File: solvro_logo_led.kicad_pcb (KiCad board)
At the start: 2 copper layers, 33 parts

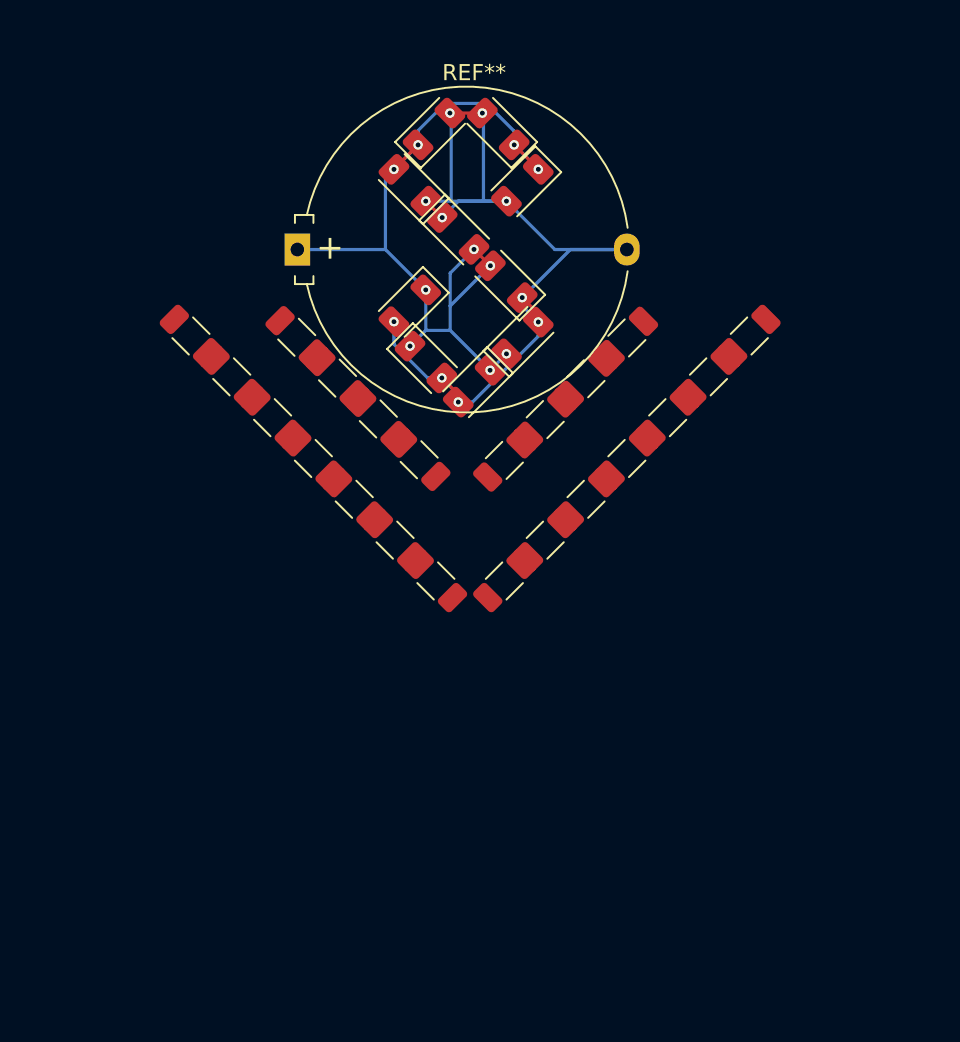
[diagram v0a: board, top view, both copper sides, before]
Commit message: Zmiany rezystorów na ledy
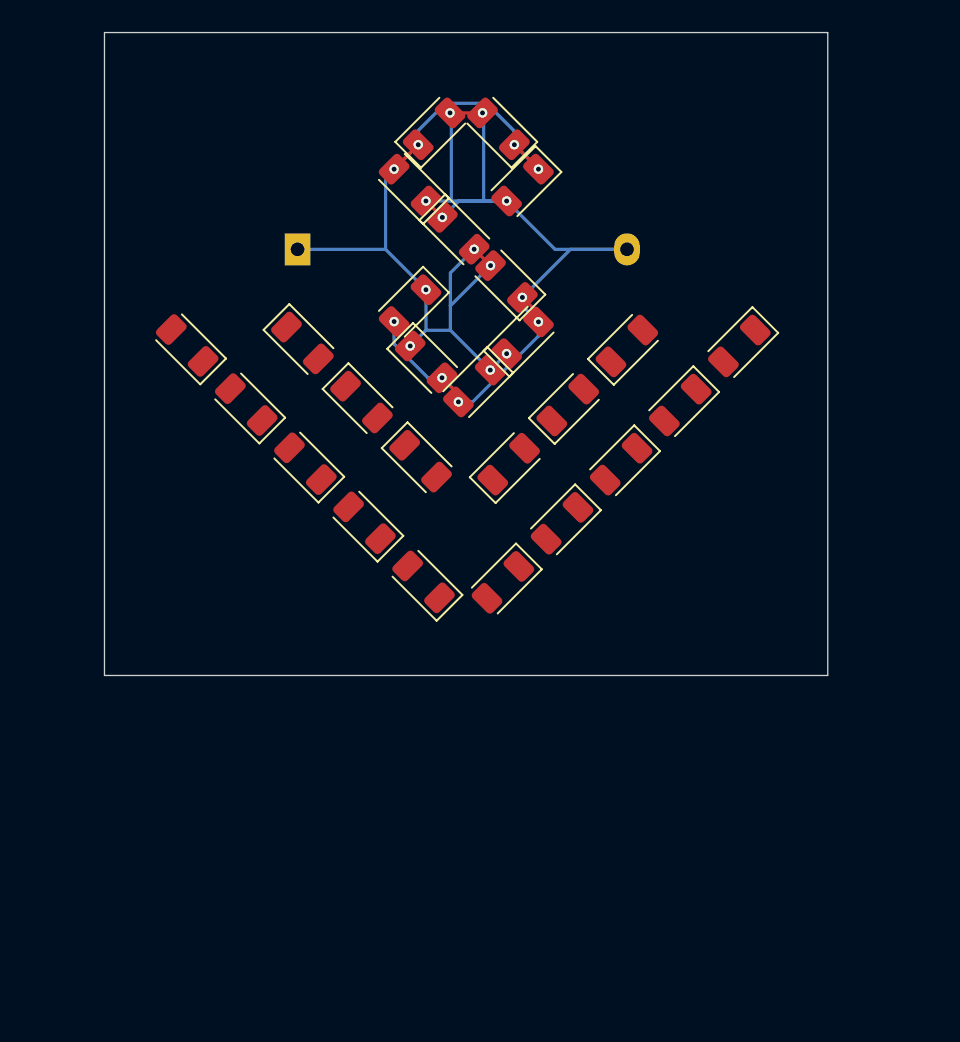
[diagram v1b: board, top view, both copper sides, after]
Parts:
- removed the REF** at (172.5, 82.0)
- removed the REF** at (167.1, 93.1)
- removed the REF** at (166.5, 83.5)
- removed the REF** at (170.5, 88.5)
- removed the REF** at (166.5, 76.0)
- removed the REF** at (173.5, 85.5)
- removed the REF** at (169.5, 79.0)
- removed the REF** at (168.1, 100.6)
- removed the REF** at (167.5, 87.0)
- removed the REF** at (172.0, 72.5)
- removed the REF** at (180.0, 85.5)
- removed the REF** at (168.0, 72.5)
- removed the REF** at (173.5, 76.0)
- removed the REF** at (187.6, 85.4)
- removed REF**1 (x2), REF**2 (x2), REF**3 (x2), REF**4 (x2), REF**5 (x2), REF**6 (x2), REF**7 (x2), REF**8 (x2), REF**9 (x2): R_1206_3216Metric, Resistor_SMD:R_1206_3216Metric
- added REF**: LED_1206_3216Metric, LED_SMD:LED_1206_3216Metric, F.Cu at (170.5, 88.5)
- added REF**: LED_1206_3216Metric, LED_SMD:LED_1206_3216Metric, F.Cu at (166.5, 83.5)
- added REF**: LED_1206_3216Metric, LED_SMD:LED_1206_3216Metric, F.Cu at (173.5, 85.5)
- added REF**: LED_1206_3216Metric, LED_SMD:LED_1206_3216Metric, F.Cu at (172.5, 82.0)
- added REF**: LED_1206_3216Metric, LED_SMD:LED_1206_3216Metric, F.Cu at (172.0, 72.5)
- added REF**: LED_1206_3216Metric, LED_SMD:LED_1206_3216Metric, F.Cu at (173.5, 76.0)
- added REF**: LED_1206_3216Metric, LED_SMD:LED_1206_3216Metric, F.Cu at (168.0, 72.5)
- added REF**: LED_1206_3216Metric, LED_SMD:LED_1206_3216Metric, F.Cu at (187.0, 86.0)
- added REF**: LED_1206_3216Metric, LED_SMD:LED_1206_3216Metric, F.Cu at (169.5, 79.0)
- added REF**: LED_1206_3216Metric, LED_SMD:LED_1206_3216Metric, F.Cu at (167.5, 87.0)
- added REF**: LED_1206_3216Metric, LED_SMD:LED_1206_3216Metric, F.Cu at (167.4, 100.7)
- added REF**: LED_1206_3216Metric, LED_SMD:LED_1206_3216Metric, F.Cu at (166.5, 76.0)
- added REF**10: LED_1206_3216Metric, LED_SMD:LED_1206_3216Metric, F.Cu at (183.3, 89.7)
- added REF**10: LED_1206_3216Metric, LED_SMD:LED_1206_3216Metric, F.Cu at (163.7, 97.0)
- added REF**11: LED_1206_3216Metric, LED_SMD:LED_1206_3216Metric, F.Cu at (179.6, 93.4)
- added REF**11: LED_1206_3216Metric, LED_SMD:LED_1206_3216Metric, F.Cu at (160.0, 93.3)
- added REF**12: LED_1206_3216Metric, LED_SMD:LED_1206_3216Metric, F.Cu at (156.3, 89.6)
- added REF**12: LED_1206_3216Metric, LED_SMD:LED_1206_3216Metric, F.Cu at (176.0, 97.0)
- added REF**13: LED_1206_3216Metric, LED_SMD:LED_1206_3216Metric, F.Cu at (180.0, 86.0)
- added REF**13: LED_1206_3216Metric, LED_SMD:LED_1206_3216Metric, F.Cu at (167.2, 93.2)
- added REF**13: LED_1206_3216Metric, LED_SMD:LED_1206_3216Metric, F.Cu at (152.6, 86.0)
- added REF**13: LED_1206_3216Metric, LED_SMD:LED_1206_3216Metric, F.Cu at (172.3, 100.7)
- added REF**14: LED_1206_3216Metric, LED_SMD:LED_1206_3216Metric, F.Cu at (163.5, 89.5)
- added REF**14: LED_1206_3216Metric, LED_SMD:LED_1206_3216Metric, F.Cu at (176.3, 89.7)
- added REF**15: LED_1206_3216Metric, LED_SMD:LED_1206_3216Metric, F.Cu at (159.8, 85.8)
- added REF**15: LED_1206_3216Metric, LED_SMD:LED_1206_3216Metric, F.Cu at (172.6, 93.4)
- REF**: moved to B.Cu
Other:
- board outline added: 45 x 40 mm

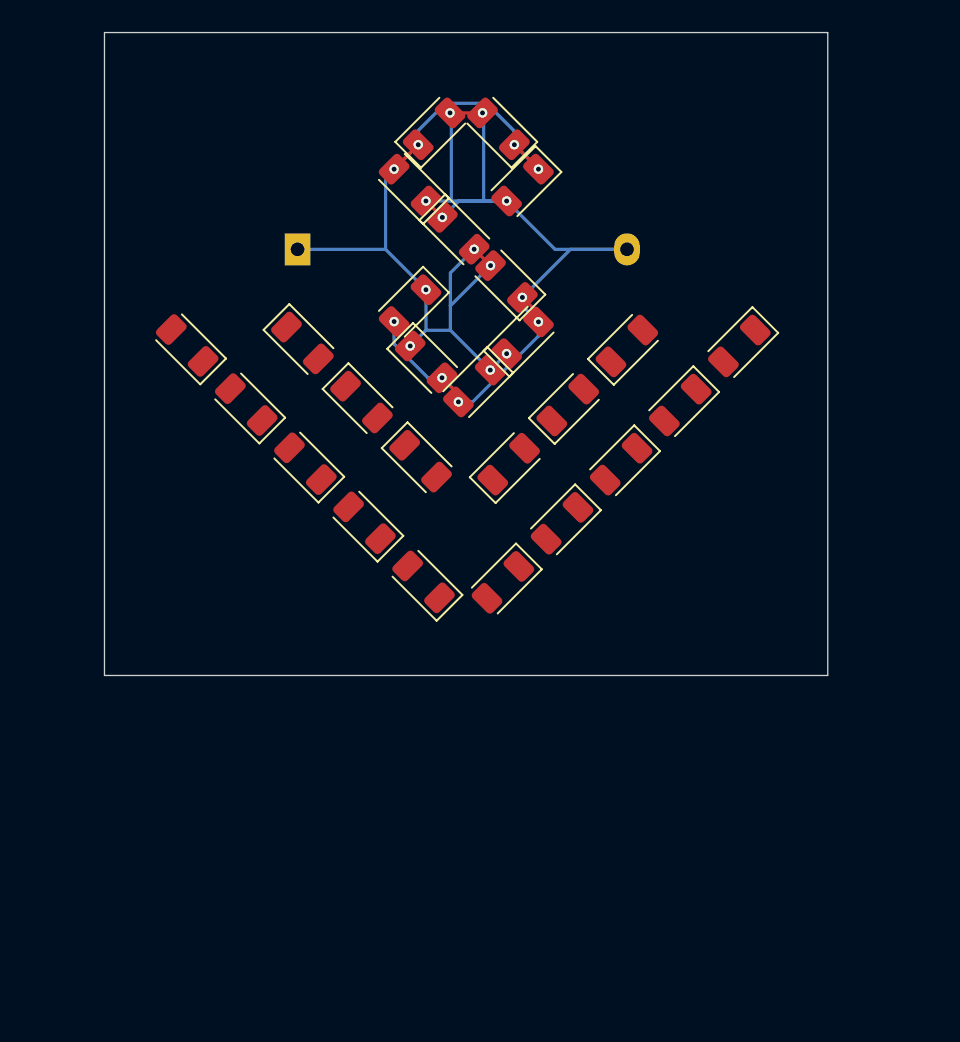
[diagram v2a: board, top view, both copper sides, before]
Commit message: Dodanie plików gerber, schematu, płytki produkcyjnej i stp
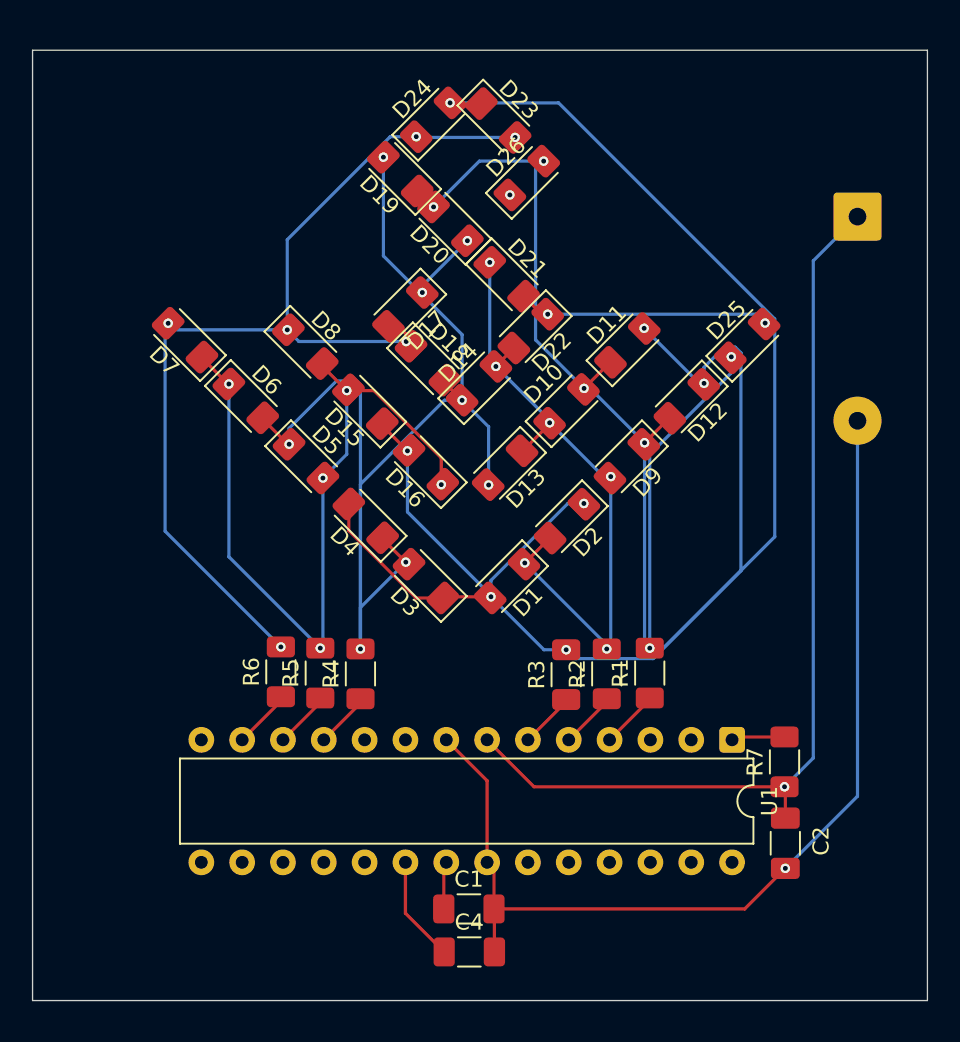
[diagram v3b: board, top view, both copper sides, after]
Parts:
- removed REF** (x12), REF**10 (x2), REF**11 (x2), REF**12 (x2), REF**13 (x4), REF**14 (x2), REF**15 (x2): LED_1206_3216Metric, LED_SMD:LED_1206_3216Metric
- removed REF**: Battery_Panasonic_CR2032-HFN_Horizontal_CircularHoles, Battery:Battery_Panasonic_CR2032-HFN_Horizontal_CircularHoles
- added BT1: 4.5V Battery, Battery:BatteryHolder_Keystone_2479_3xAAA, B.Cu at (194.3, 78.0)
- added C1: 100nF, Capacitor_SMD:C_1206_3216Metric_Pad1.33x1.80mm_HandSolder, F.Cu at (170.2, 121.0)
- added C2: 100nF, Capacitor_SMD:C_1206_3216Metric_Pad1.33x1.80mm_HandSolder, F.Cu at (189.9, 116.9)
- added C4: 10uF, Capacitor_SMD:C_1206_3216Metric_Pad1.33x1.80mm_HandSolder, F.Cu at (170.2, 123.7)
- added D1: LED, LED_SMD:LED_1206_3216Metric_Pad1.42x1.75mm_HandSolder, F.Cu at (172.5, 100.6)
- added D10: LED, LED_SMD:LED_1206_3216Metric_Pad1.42x1.75mm_HandSolder, F.Cu at (176.2, 89.8)
- added D11: LED, LED_SMD:LED_1206_3216Metric_Pad1.42x1.75mm_HandSolder, F.Cu at (180.0, 86.0)
- added D12: LED, LED_SMD:LED_1206_3216Metric_Pad1.42x1.75mm_HandSolder, F.Cu at (183.7, 89.4)
- added D13: LED, LED_SMD:LED_1206_3216Metric_Pad1.42x1.75mm_HandSolder, F.Cu at (172.4, 93.6)
- added D14: LED, LED_SMD:LED_1206_3216Metric_Pad1.42x1.75mm_HandSolder, F.Cu at (170.8, 88.3)
- added D15: LED, LED_SMD:LED_1206_3216Metric_Pad1.42x1.75mm_HandSolder, F.Cu at (163.7, 89.8)
- added D16: LED, LED_SMD:LED_1206_3216Metric_Pad1.42x1.75mm_HandSolder, F.Cu at (167.5, 93.5)
- added D17: LED, LED_SMD:LED_1206_3216Metric_Pad1.42x1.75mm_HandSolder, F.Cu at (166.2, 83.7)
- added D18: LED, LED_SMD:LED_1206_3216Metric_Pad1.42x1.75mm_HandSolder, F.Cu at (167.6, 87.1)
- added D19: LED, LED_SMD:LED_1206_3216Metric_Pad1.42x1.75mm_HandSolder, F.Cu at (165.9, 75.3)
- added D2: LED, LED_SMD:LED_1206_3216Metric_Pad1.42x1.75mm_HandSolder, F.Cu at (176.3, 96.9)
- added D20: LED, LED_SMD:LED_1206_3216Metric_Pad1.42x1.75mm_HandSolder, F.Cu at (169.0, 78.4)
- added D21: LED, LED_SMD:LED_1206_3216Metric_Pad1.42x1.75mm_HandSolder, F.Cu at (172.5, 81.8)
- added D22: LED, LED_SMD:LED_1206_3216Metric_Pad1.42x1.75mm_HandSolder, F.Cu at (174.0, 85.1)
- added D23: LED, LED_SMD:LED_1206_3216Metric_Pad1.42x1.75mm_HandSolder, F.Cu at (172.0, 72.0)
- added D24: LED, LED_SMD:LED_1206_3216Metric_Pad1.42x1.75mm_HandSolder, F.Cu at (167.9, 71.9)
- added D25: LED, LED_SMD:LED_1206_3216Metric_Pad1.42x1.75mm_HandSolder, F.Cu at (187.5, 85.7)
- added D26: LED, LED_SMD:LED_1206_3216Metric_Pad1.42x1.75mm_HandSolder, F.Cu at (173.8, 75.6)
- added D3: LED, LED_SMD:LED_1206_3216Metric_Pad1.42x1.75mm_HandSolder, F.Cu at (167.5, 100.6)
- added D4: LED, LED_SMD:LED_1206_3216Metric_Pad1.42x1.75mm_HandSolder, F.Cu at (163.8, 96.9)
- added D5: LED, LED_SMD:LED_1206_3216Metric_Pad1.42x1.75mm_HandSolder, F.Cu at (160.0, 93.2)
- added D6: LED, LED_SMD:LED_1206_3216Metric_Pad1.42x1.75mm_HandSolder, F.Cu at (156.3, 89.4)
- added D7: LED, LED_SMD:LED_1206_3216Metric_Pad1.42x1.75mm_HandSolder, F.Cu at (152.5, 85.6)
- added D8: LED, LED_SMD:LED_1206_3216Metric_Pad1.42x1.75mm_HandSolder, F.Cu at (160.0, 86.0)
- added D9: LED, LED_SMD:LED_1206_3216Metric_Pad1.42x1.75mm_HandSolder, F.Cu at (180.0, 93.2)
- added R1: 47R, Resistor_SMD:R_1206_3216Metric_Pad1.30x1.75mm_HandSolder, F.Cu at (181.4, 106.3)
- added R2: 47R, Resistor_SMD:R_1206_3216Metric_Pad1.30x1.75mm_HandSolder, F.Cu at (178.8, 106.4)
- added R3: 47R, Resistor_SMD:R_1206_3216Metric_Pad1.30x1.75mm_HandSolder, F.Cu at (176.2, 106.5)
- added R4: 47R, Resistor_SMD:R_1206_3216Metric_Pad1.30x1.75mm_HandSolder, F.Cu at (163.4, 106.4)
- added R5: 47R, Resistor_SMD:R_1206_3216Metric_Pad1.30x1.75mm_HandSolder, F.Cu at (160.9, 106.3)
- added R6: 47R, Resistor_SMD:R_1206_3216Metric_Pad1.30x1.75mm_HandSolder, F.Cu at (158.5, 106.3)
- added R7: 10K, Resistor_SMD:R_1206_3216Metric_Pad1.30x1.75mm_HandSolder, F.Cu at (189.8, 111.9)
- added U1: ATmega328-P, Package_DIP:DIP-28_W7.62mm, F.Cu at (186.5, 110.5)
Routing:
- net Net-(D1-A): track 0.00 -> 127.8 mm, vias 0 -> 7
- net Net-(D13-A): track 0.00 -> 83.5 mm, vias 0 -> 8
- net Net-(D10-A): track 0.00 -> 68.0 mm, vias 0 -> 6
- net Net-(D15-A): track 0.00 -> 66.0 mm, vias 0 -> 8
- net Net-(BT1-+): track 0.00 -> 65.6 mm, vias 0 -> 1
- net Net-(BT1--): track 0.00 -> 63.3 mm, vias 0 -> 1
- net Net-(D17-A): track 0.00 -> 63.1 mm, vias 0 -> 6
- net LED-: track 60.9 -> 0.00 mm, vias 10 -> 0
- net LED+: track 52.9 -> 0.00 mm, vias 10 -> 0
- net Net-(D1-K): track 0.00 -> 41.3 mm, vias 0 -> 6
- net F: track 0.00 -> 3.68 mm
- net A: track 0.00 -> 3.64 mm
- net E: track 0.00 -> 3.57 mm
- net B: track 0.00 -> 3.53 mm
- net D: track 0.00 -> 3.50 mm
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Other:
- board size 45 x 40 mm -> 55.7 x 59.1 mm

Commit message: export to gerber
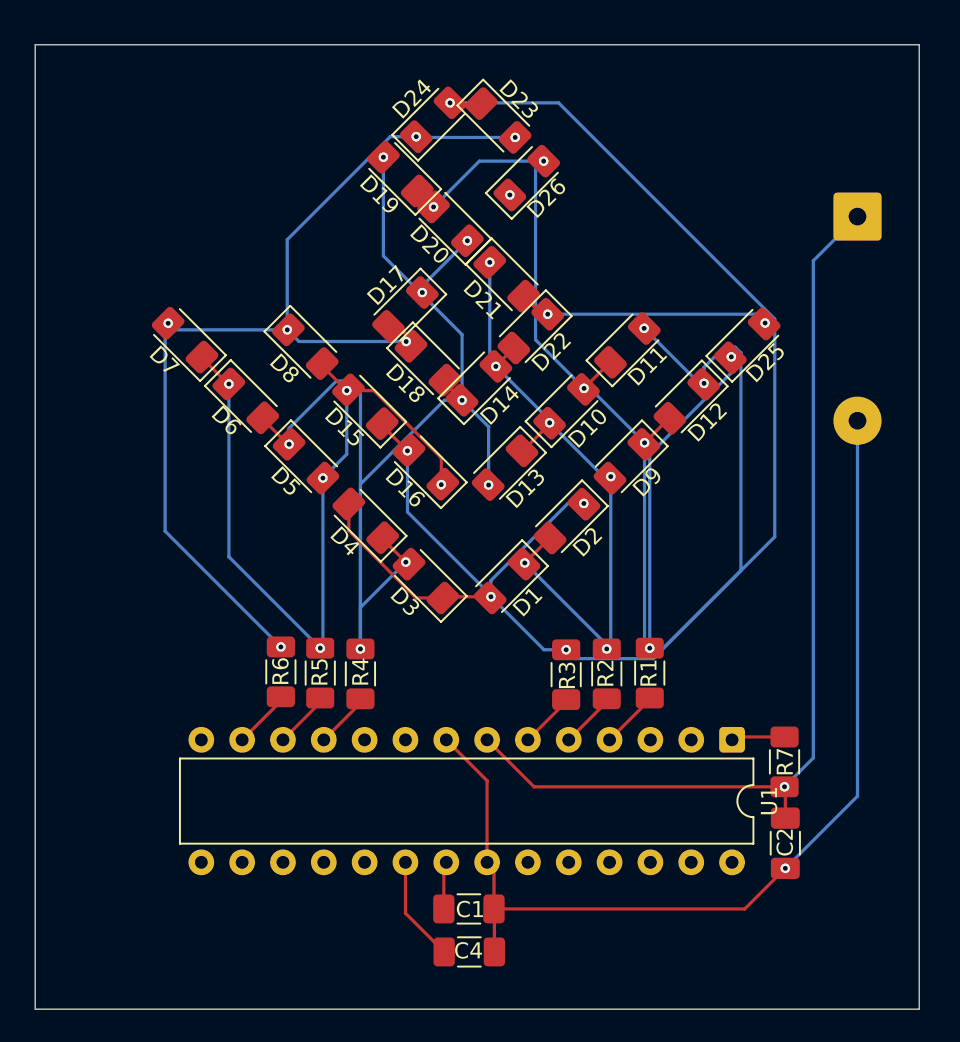
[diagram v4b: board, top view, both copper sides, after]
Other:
- board size 55.7 x 59.1 mm -> 55 x 60 mm
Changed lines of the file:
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@@
 		(tags "resistor handsolder")
 		(property "Reference" "R4"
-			(at 0 -1.829999 90)
+			(at 0.11 0.025 90)
 			(layer "F.SilkS")
 			(effects
@@
 		(tags "LED handsolder")
 		(property "Reference" "D21"
-			(at 0 -1.829999 135)
+			(at -0.128239 1.941008 135)
 			(layer "F.SilkS")
 			(effects
@@
 		(tags "LED handsolder")
 		(property "Reference" "D25"
-			(at 0 -1.829999 45)
+			(at -0.136848 1.778374 45)
 			(layer "F.SilkS")
 			(effects
@@
 		(tags "resistor handsolder")
 		(property "Reference" "R6"
-			(at 0 -1.829999 90)
+			(at 0.025 0.005 90)
 			(layer "F.SilkS")
 			(effects
@@
 		(tags "resistor handsolder")
 		(property "Reference" "R3"
-			(at 0 -1.829999 90)
+			(at -0.06 0.085 90)
 			(layer "F.SilkS")
 			(effects
@@
 		(tags "LED handsolder")
 		(property "Reference" "D17"
-			(at 0 -1.829999 45)
+			(at -0.250063 1.85262 45)
 			(layer "F.SilkS")
 			(effects
@@
 		(tags "capacitor handsolder")
 		(property "Reference" "C2"
-			(at -0.1375 -2.225 90)
+			(at -0.0675 0 90)
 			(layer "F.SilkS")
 			(effects
@@
 		(tags "LED handsolder")
 		(property "Reference" "D8"
-			(at 0 -1.829999 135)
+			(at 0.057222 1.887975 135)
 			(layer "F.SilkS")
 			(effects
@@
 		(tags "LED handsolder")
 		(property "Reference" "D11"
-			(at 0 -1.829999 45)
+			(at -0.019598 1.796051 45)
 			(layer "F.SilkS")
 			(effects
@@
 		(tags "LED handsolder")
 		(property "Reference" "D10"
-			(at -0.015102 -1.997577 45)
+			(at -0.014622 1.916259 45)
 			(layer "F.SilkS")
 			(effects
@@
 		(tags "resistor handsolder")
 		(property "Reference" "R5"
-			(at 0 -1.829999 90)
+			(at 0.06 -0.015 90)
 			(layer "F.SilkS")
 			(effects
@@
 		(tags "LED handsolder")
 		(property "Reference" "D5"
-			(at 0 -1.829999 135)
+			(at 0.010761 1.792516 135)
 			(layer "F.SilkS")
 			(effects
@@
 		(tags "capacitor handsolder")
 		(property "Reference" "C4"
-			(at 0 -1.850001 0)
+			(at -0.0475 -0.06 0)
 			(layer "F.SilkS")
 			(effects
@@
 		(tags "capacitor handsolder")
 		(property "Reference" "C1"
-			(at 0 -1.850001 0)
+			(at 0.0875 0.045 0)
 			(layer "F.SilkS")
 			(effects
@@
 		(tags "LED handsolder")
 		(property "Reference" "D18"
-			(at 0 -1.829999 135)
+			(at -0.089349 1.880904 135)
 			(layer "F.SilkS")
 			(effects
@@
 		(tags "resistor handsolder")
 		(property "Reference" "R7"
-			(at 0 -1.829999 90)
+			(at 0.005 0.05 90)
 			(layer "F.SilkS")
 			(effects
@@
 		(tags "resistor handsolder")
 		(property "Reference" "R1"
-			(at 0 -1.829999 90)
+			(at -0.01 -0.045 90)
 			(layer "F.SilkS")
 			(effects
@@
 		(tags "LED handsolder")
 		(property "Reference" "D14"
-			(at 0 -1.829999 45)
+			(at -0.03182 1.898582 45)
 			(layer "F.SilkS")
 			(effects
@@
 		(tags "LED handsolder")
 		(property "Reference" "D6"
-			(at 0 -1.829999 135)
+			(at 0.020483 1.735947 135)
 			(layer "F.SilkS")
 			(effects
@@
 		(tags "LED handsolder")
 		(property "Reference" "D26"
-			(at 0 -1.829999 45)
+			(at -0.015102 1.778374 45)
 			(layer "F.SilkS")
 			(effects
@@
 		(tags "resistor handsolder")
 		(property "Reference" "R2"
-			(at 0 -1.829999 90)
+			(at 0.04 -0.05 90)
 			(layer "F.SilkS")
 			(effects
@@
 	)
 	(gr_rect
-		(start 143.025 67.6)
-		(end 198.7 126.725)
+		(start 143.19 67.26)
+		(end 198.19 127.26)
 		(stroke
 			(width 0.05)
-			(type default)
+			(type solid)
 		)
 		(fill no)
